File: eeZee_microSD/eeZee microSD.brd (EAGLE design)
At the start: 20.2 x 29.2 mm, 12 parts, among them U1 MCP1824S, U2 74HC4050

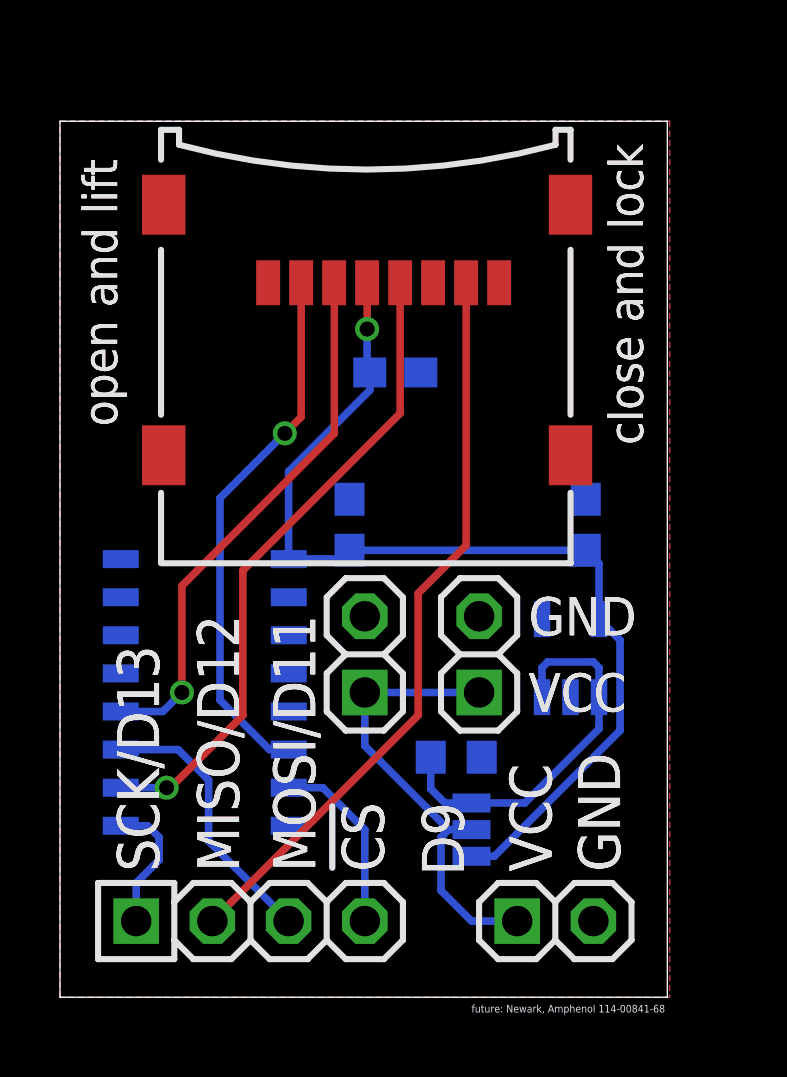
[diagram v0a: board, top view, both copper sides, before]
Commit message: Layout tweaks to fix power pin alignment.
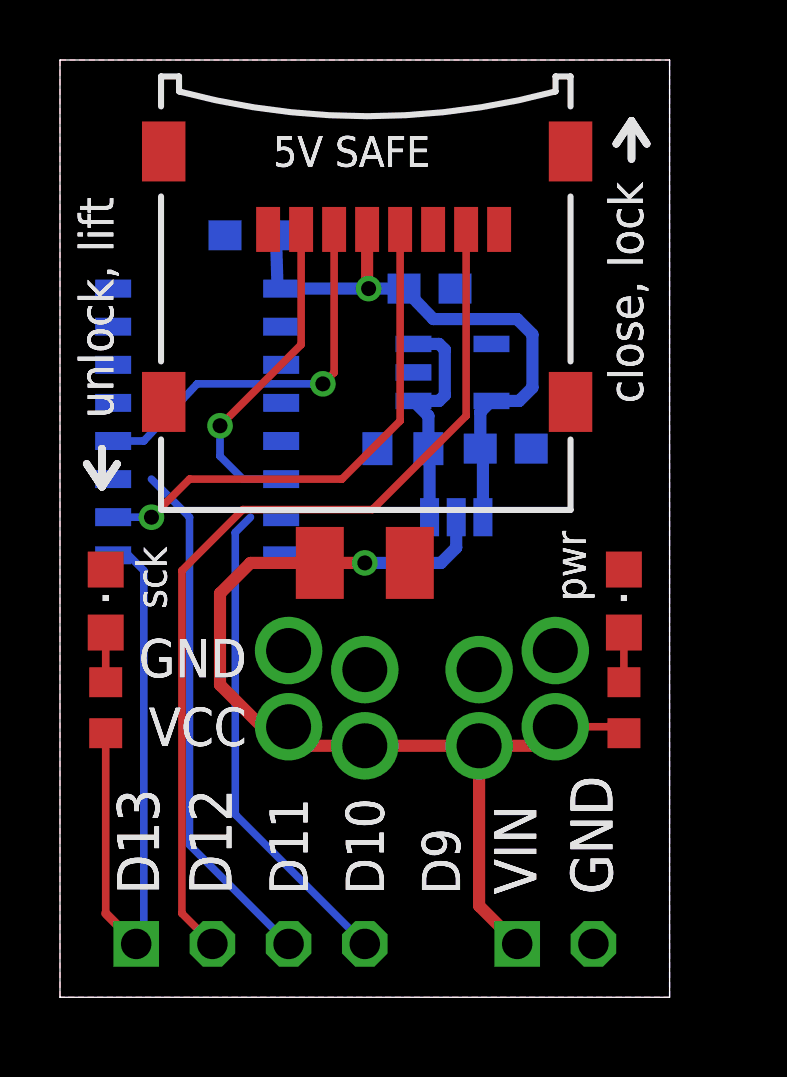
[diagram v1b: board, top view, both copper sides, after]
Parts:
- added C4: 10uF, rcl:SMC_B
- added JP4: PWR, mes_electromech:BIGPIN-2
- added JP6: (no value), pinhead-2:1X04-S
- added LED1, LED2: (no value), mes_opto:CHIPLED_0805
- added R1, R2: 1K, rcl:R0603
- JP2, JP3: value (none) -> PWR; device pinhead-2:1X02-S -> mes_electromech:BIGPIN-2
- JP5: value (none) -> PWR; device pinhead-2:1X04-S -> mes_electromech:BIGPIN-2
- moved R5 10.4 mm to (11.4, 18.3), turned to 180 degrees
- moved REG 10.4 mm to (13.2, 16.0), turned to 0 degrees
- moved U1 10.3 mm to (13.1, 20.8), turned to 90 degrees
- moved C1 9.44 mm to (12.3, 23.6), turned to 180 degrees
- moved U2 9.02 mm to (4.57, 19.2)
- moved JP2 6.79 mm to (16.5, 9.02), flipped to the bottom
- moved C2 6.65 mm to (6.35, 25.4), turned to 0 degrees
- moved JP5 6.60 mm to (7.62, 9.02), flipped to the bottom, turned to 90 degrees
- moved C3 5.79 mm to (14.9, 18.3), turned to 180 degrees
- moved JP3 4.88 mm to (10.2, 8.38), flipped to the bottom
- moved U$1 1.78 mm to (17.0, 28.2)
- moved JP1 0.76 mm to (16.5, 1.78), flipped to the bottom, turned to 180 degrees
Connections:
- net VIN renamed VREGIN
- removed net VOUT: C1.1, C2.1, C3.1, REG.1, U$1.VDD, U1.5, U2.1
- new net N$1: LED2.A, R2.1
- new net N$2: LED1.A, R1.1
- new net VBOARD: C4.+, JP1.1, JP2.P$1, JP3.P$1, JP4.P$1, JP5.P$1, R2.2, REG.2
- net !CS_HV: now also JP6.4; no longer JP5.4
- net GND: now also C4.-, JP2.P$2, JP3.P$2, JP4.P$2, JP5.P$2, LED1.C, LED2.C; no longer JP2.2, JP3.2
- net MISO: now also JP6.2; no longer JP5.2
- net MOSI_HV: now also JP6.3; no longer JP5.3
- net SCK_HV: now also JP6.1, R1.2; no longer JP5.1
- net VCC: now also C1.1, C2.1, C3.1, REG.1, U$1.VDD, U1.5, U2.1; no longer JP1.1, JP2.1, JP3.1, REG.2
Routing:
- net VBOARD: track 0.00 -> 34.4 mm, vias 0 -> 1
- net VOUT: track 33.6 -> 0.00 mm, vias 1 -> 0
- net SCK_HV: track 4.54 -> 21.2 mm
- net !CS_HV: track 6.16 -> 16.2 mm
- net MOSI_HV: track 9.15 -> 17.4 mm
- net !SS: track 18.0 -> 11.0 mm
- net MISO: track 24.8 -> 30.7 mm
- net VREGIN: track 13.0 -> 7.87 mm
- net MOSI: track 18.1 -> 13.1 mm
- net VCC: track 15.4 -> 20.2 mm, vias 0 -> 1
- net SCK: track 21.7 -> 17.3 mm
- net N$2: track 0.00 -> 1.66 mm
- net N$1: track 0.00 -> 1.66 mm
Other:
- board size 20.2 x 29.2 mm -> 20.3 x 31.2 mm
- board text added: "5V SAFE"
- board text added: "D10"
- board text added: "D11"
- board text added: "D12"
- board text added: "D13"
- board text added: "JP2"
- board text added: "MISO"
- board text added: "MOSI"
- board text added: "R0.2"
- board text added: "SCK"
- board text added: "VIN"
- board text added: "close, lock"
- board text added: "pwr"
- board text added: "sck"
- board text added: "unlock, lift"
- board text removed: "MISO/D12"
- board text removed: "MOSI/D11"
- board text removed: "R0.1"
- board text removed: "SCK/D13"
- board text removed: "close and lock"
- board text removed: "future: Newark, Amphenol 114-00841-68"
- board text removed: "open and lift"

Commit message: Fixes to PropVGA, microSD,
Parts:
- removed LED1, LED2: (no value), mes_opto:CHIPLED_0805
- removed R1, R2: 1K, rcl:R0603
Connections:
- removed net N$1: LED2.A, R2.1
- removed net N$2: LED1.A, R1.1
- net GND: no longer LED1.C, LED2.C
- net SCK_HV: no longer R1.2
- net VBOARD: no longer R2.2
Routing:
- net SCK_HV: track 21.2 -> 13.8 mm
- net VBOARD: track 34.4 -> 32.0 mm
- net N$2: track 1.66 -> 0.00 mm
- net N$1: track 1.66 -> 0.00 mm
- net MOSI_HV: track 17.4 -> 18.7 mm
- net !CS_HV: track 16.2 -> 17.2 mm
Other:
- board text removed: "JP2"
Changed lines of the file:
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@@
 <layer number="26" name="bNames" color="7" fill="1" visible="no" active="yes"/>
 <layer number="27" name="tValues" color="7" fill="1" visible="no" active="yes"/>
-<layer number="28" name="bValues" color="7" fill="1" visible="yes" active="yes"/>
-<layer number="29" name="tStop" color="7" fill="3" visible="yes" active="yes"/>
-<layer number="30" name="bStop" color="7" fill="6" visible="yes" active="yes"/>
+<layer number="28" name="bValues" color="7" fill="1" visible="no" active="yes"/>
+<layer number="29" name="tStop" color="7" fill="3" visible="no" active="yes"/>
+<layer number="30" name="bStop" color="7" fill="6" visible="no" active="yes"/>
 <layer number="31" name="tCream" color="7" fill="4" visible="no" active="yes"/>
 <layer number="32" name="bCream" color="7" fill="5" visible="no" active="yes"/>
@@
 <layer number="107" name="Crop" color="7" fill="1" visible="no" active="yes"/>
 <layer number="116" name="Patch_BOT" color="9" fill="4" visible="no" active="yes"/>
-<layer number="121" name="_tsilk" color="14" fill="1" visible="yes" active="yes"/>
-<layer number="122" name="_bsilk" color="6" fill="1" visible="yes" active="yes"/>
+<layer number="121" name="_tsilk" color="14" fill="1" visible="no" active="yes"/>
+<layer number="122" name="_bsilk" color="6" fill="1" visible="no" active="yes"/>
 <layer number="125" name="_tNames" color="7" fill="1" visible="no" active="yes"/>
 <layer number="144" name="Drill_legend" color="7" fill="1" visible="no" active="yes"/>
@@
 <wire x1="19.05" y1="29.21" x2="18.542" y2="28.448" width="0.254" layer="121"/>
 <wire x1="19.558" y1="28.448" x2="19.05" y2="29.21" width="0.254" layer="121"/>
-<rectangle x1="1.424" y1="13.208" x2="1.624" y2="13.408" layer="121"/>
-<rectangle x1="18.696" y1="13.208" x2="18.896" y2="13.408" layer="121"/>
 <wire x1="17.018" y1="26.694003125" x2="17.018" y2="21.1939875" width="0.2032" layer="121"/>
 <wire x1="17.018" y1="16.2440125" x2="3.367990625" y2="16.2440125" width="0.2032" layer="121"/>
@@
 <text x="8.255" y="24.765" size="1.016" layer="122" font="vector" ratio="20" rot="MR90">C2</text>
 <text x="16.637" y="17.526" size="1.016" layer="122" font="vector" ratio="20" rot="MR90">C3</text>
-<text x="18.415" y="7.747" size="1.27" layer="122" font="vector" ratio="16" rot="MR90">JP2</text>
 <text x="9.652" y="19.304" size="1.016" layer="122" font="vector" ratio="20" rot="MR270">R5</text>
 <text x="11.303" y="15.621" size="1.016" layer="122" font="vector" ratio="20" rot="MR0">REG</text>
@@
 <attribute name="DATABASE" value="./../../../eagle/PARTSDB.TXT" x="10.16" y="14.478" size="1.778" layer="27" display="off"/>
 </element>
-<element name="LED1" library="mes_opto" package="CHIPLED_0805" value="" x="1.524" y="13.208" smashed="yes">
-<attribute name="VALUE" x="4.064" y="11.938" size="1.27" layer="27" rot="R90"/>
-</element>
-<element name="R1" library="rcl" package="R0603" value="1K" x="1.524" y="9.652" smashed="yes" rot="R270">
-<attribute name="PARTNO" value="ERJ-3GEYJ103V" x="1.524" y="9.652" size="1.778" layer="27" rot="R270" display="off"/>
-<attribute name="DATABASE" value="./../../../eagle/PARTSDB.TXT" x="1.524" y="9.652" size="1.778" layer="27" rot="R270" display="off"/>
-</element>
 <element name="JP3" library="mes_electromech" package="BIGPIN-2" value="PWR" x="10.16" y="8.382" smashed="yes" rot="MR90"/>
 <element name="JP2" library="mes_electromech" package="BIGPIN-2" value="PWR" x="16.51" y="9.017" smashed="yes" rot="MR90">
@@
 <element name="JP4" library="mes_electromech" package="BIGPIN-2" value="PWR" x="13.97" y="8.382" smashed="yes" rot="MR90">
 <attribute name="DATABASE" value="./../../../eagle/PARTSDB.TXT" x="13.97" y="8.382" size="1.778" layer="28" rot="MR90" display="off"/>
-</element>
-<element name="R2" library="rcl" package="R0603" value="1K" x="18.796" y="9.652" smashed="yes" rot="R270">
-<attribute name="PARTNO" value="ERJ-3GEYJ103V" x="18.796" y="9.652" size="1.778" layer="27" rot="R270" display="off"/>
-<attribute name="DATABASE" value="./../../../eagle/PARTSDB.TXT" x="18.796" y="9.652" size="1.778" layer="27" rot="R270" display="off"/>
-</element>
-<element name="LED2" library="mes_opto" package="CHIPLED_0805" value="" x="18.796" y="13.208" smashed="yes">
-<attribute name="DATABASE" value="./../../../eagle/PARTSDB.TXT" x="18.796" y="13.208" size="1.778" layer="27" display="off"/>
-<attribute name="VALUE" x="21.336" y="11.938" size="1.27" layer="27" rot="R90"/>
 </element>
 </elements>
@@
 <contactref element="JP6" pad="1"/>
 <contactref element="U2" pad="9"/>
-<wire x1="1.524" y1="2.794" x2="2.54" y2="1.778" width="0.3048" layer="1"/>
 <wire x1="1.772" y1="14.732" x2="2.286" y2="14.732" width="0.254" layer="16"/>
 <wire x1="2.286" y1="14.732" x2="2.794" y2="14.224" width="0.254" layer="16"/>
 <wire x1="2.794" y1="14.224" x2="2.794" y2="2.032" width="0.254" layer="16"/>
 <wire x1="2.794" y1="2.032" x2="2.54" y2="1.778" width="0.254" layer="16"/>
-<contactref element="R1" pad="2"/>
-<wire x1="1.524" y1="8.802" x2="1.524" y2="2.794" width="0.254" layer="1"/>
 </signal>
 <signal name="MOSI">
@@
 <contactref element="U$1" pad="SHIELD3"/>
 <contactref element="U$1" pad="SHIELD4"/>
-<contactref element="LED2" pad="C"/>
-<contactref element="LED1" pad="C"/>
 </signal>
 <signal name="MOSI_HV">
@@
 <wire x1="4.318" y1="5.08" x2="7.62" y2="1.778" width="0.254" layer="16"/>
 <contactref element="U2" pad="11"/>
-<wire x1="3.048" y1="17.272" x2="1.772" y2="17.272" width="0" layer="19" extent="16-16"/>
+<wire x1="3.048" y1="17.272" x2="1.772" y2="17.272" width="0.254" layer="16"/>
 </signal>
 <signal name="VBOARD">
@@
 <wire x1="12.7" y1="14.478" x2="13.208" y2="14.986" width="0.4064" layer="16"/>
 <wire x1="13.208" y1="14.986" x2="13.208" y2="16.002" width="0.4064" layer="16"/>
-<contactref element="R2" pad="2"/>
-<wire x1="16.51" y1="9.017" x2="18.581" y2="9.017" width="0.254" layer="1"/>
-<wire x1="18.581" y1="9.017" x2="18.796" y2="8.802" width="0.254" layer="1"/>
 </signal>
 <signal name="VREGIN">
@@
 <wire x1="5.842" y1="15.494" x2="6.35" y2="16.002" width="0.254" layer="16"/>
 <contactref element="U2" pad="7"/>
-<wire x1="6.35" y1="16.002" x2="7.372" y2="16.002" width="0" layer="19" extent="16-16"/>
+<wire x1="7.372" y1="16.002" x2="6.35" y2="16.002" width="0.254" layer="16"/>
 </signal>
 <signal name="VCC">
@@
 <wire x1="7.245" y1="23.831" x2="7.2" y2="25.4" width="0.4064" layer="16"/>
 </signal>
-<signal name="N$1">
-<contactref element="LED2" pad="A"/>
-<contactref element="R2" pad="1"/>
-<wire x1="18.796" y1="12.158" x2="18.796" y2="10.502" width="0.254" layer="1"/>
-</signal>
-<signal name="N$2">
-<contactref element="LED1" pad="A"/>
-<contactref element="R1" pad="1"/>
-<wire x1="1.524" y1="10.502" x2="1.524" y2="12.158" width="0.254" layer="1"/>
-</signal>
 </signals>
